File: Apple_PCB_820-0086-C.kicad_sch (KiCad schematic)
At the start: 0 parts

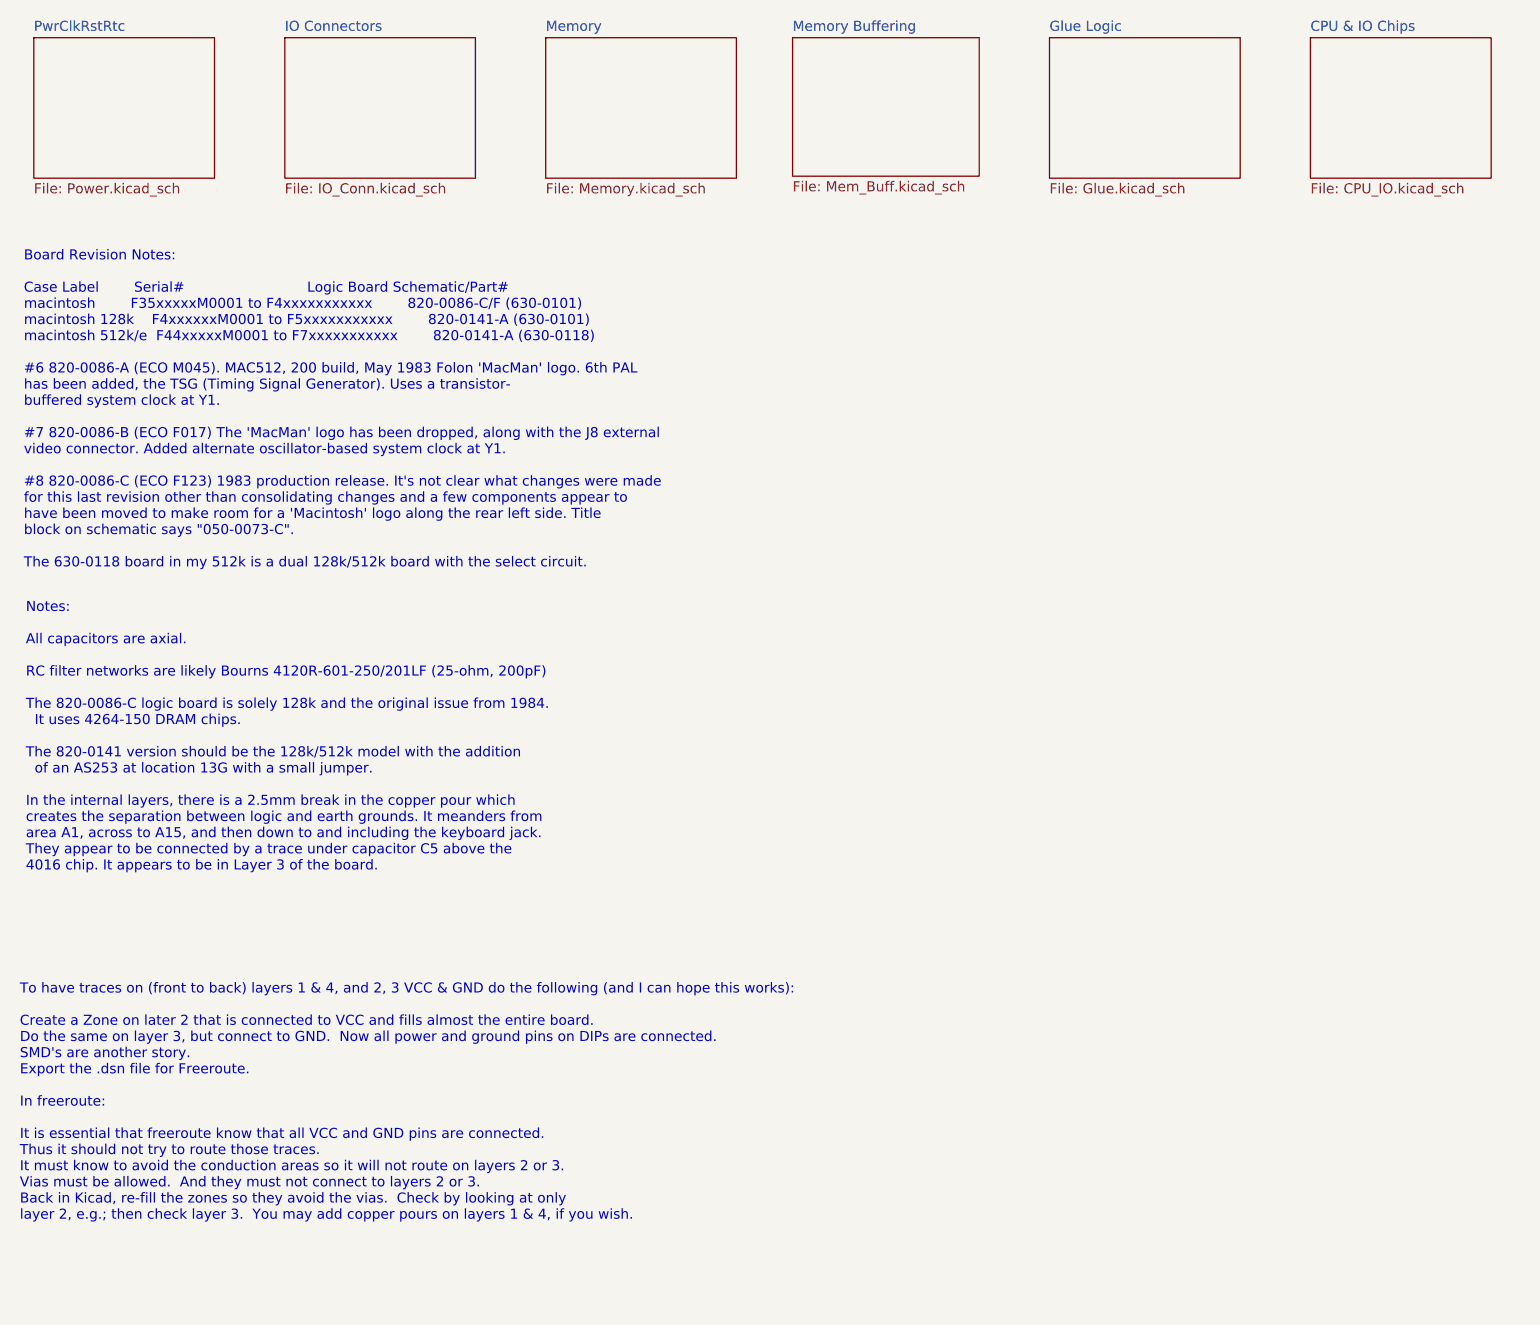
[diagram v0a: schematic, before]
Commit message: Add files via upload
After obtaining actual  128k board, certain component placement tweaks were made. Board was re-routed based on those changes.
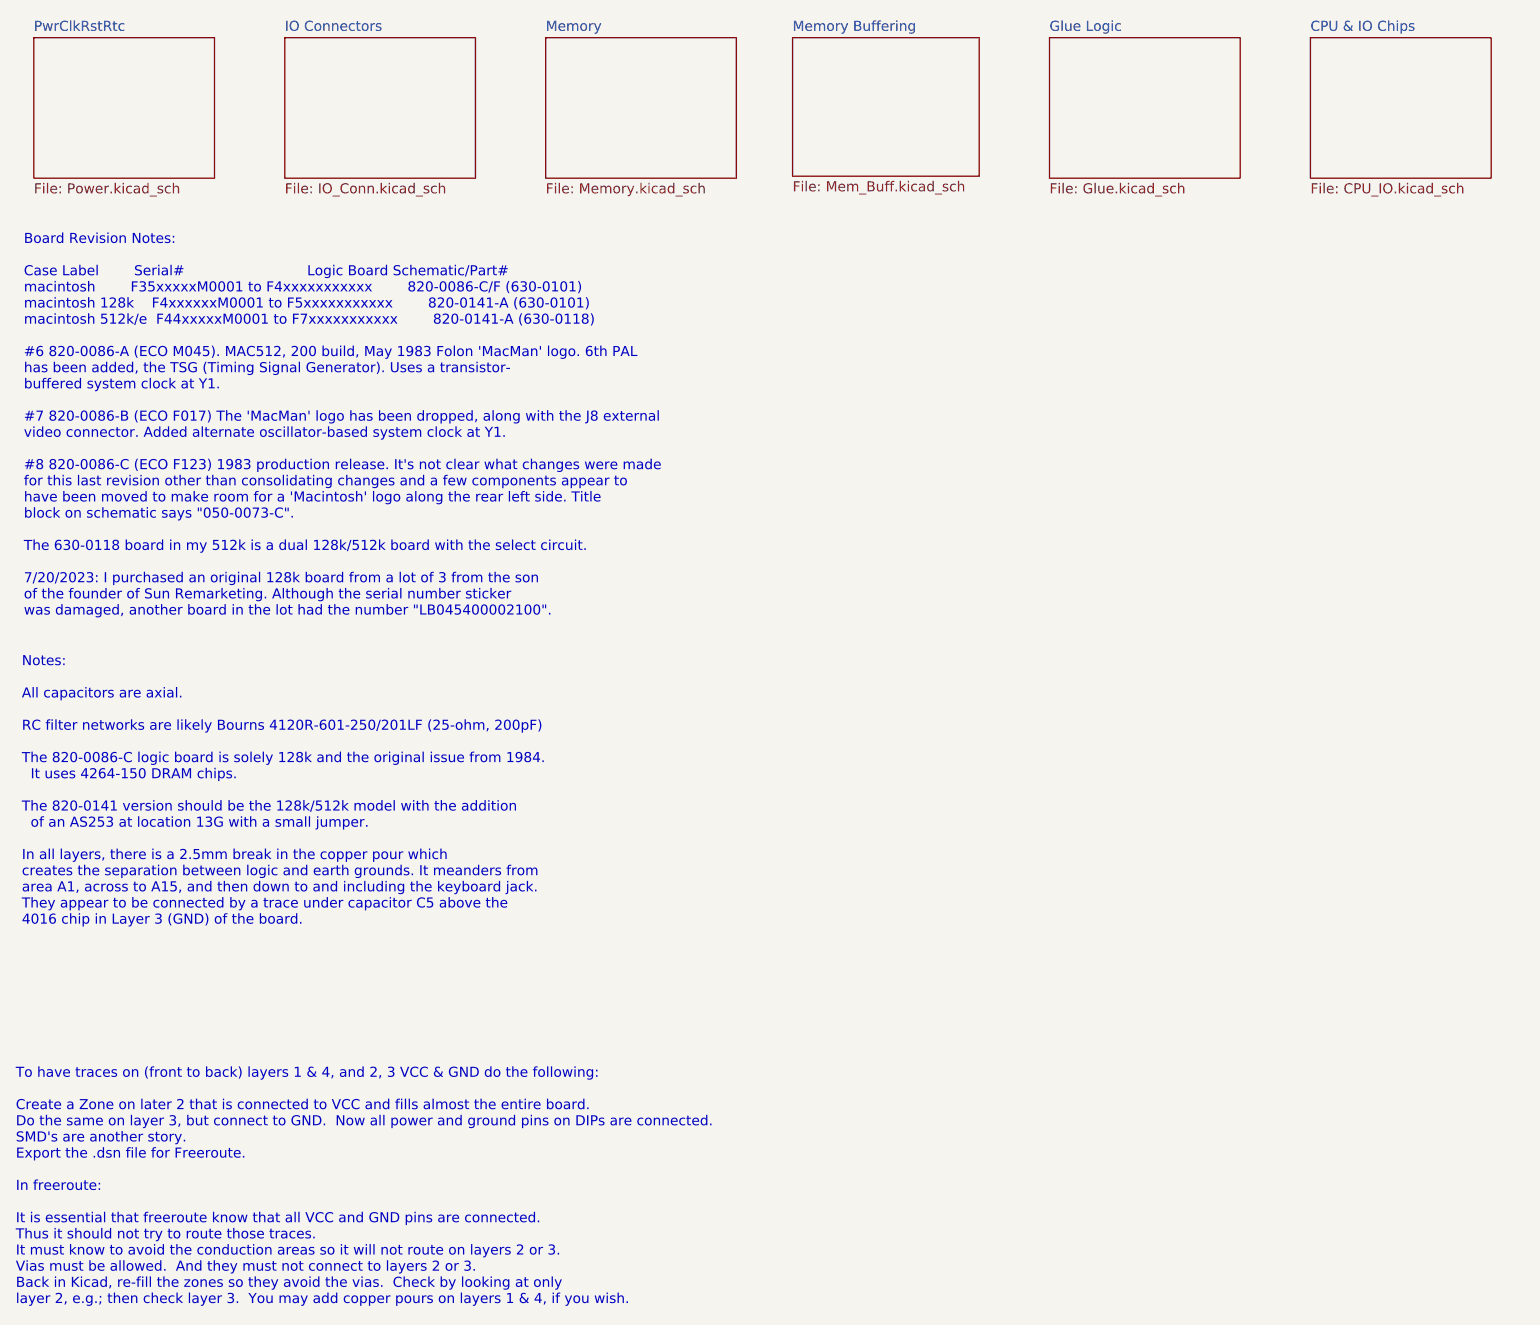
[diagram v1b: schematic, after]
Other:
- note added: "Notes: All capacitors are axial. RC filter networks are likely Bourns 4120R-601-250/201LF (25-ohm, 200pF) The 820-0086-C logic board is solely 128k and the original issue from 1984. It uses 4264-150 DRAM chips. The 820-0141 version should be the 128k/512k model with the addition of an AS253 at location 13G with a small jumper. In all layers, there is a 2.5mm break in the copper pour which creates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"
- note added: "To have traces on (front to back) layers 1 & 4, and 2, 3 VCC & GND do the following: Create a Zone on later 2 that is connected to VCC and fills almost the entire board. Do the same on layer 3, but connect to GND. Now all power and ground pins on DIPs are connected. SMD's are another story. Export the .dsn file for Freeroute. In freeroute: It is essential that freeroute know that all VCC and GND 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"
- note removed: "Notes: All capacitors are axial. RC filter networks are likely Bourns 4120R-601-250/201LF (25-ohm, 200pF) The 820-0086-C logic board is solely 128k and the original issue from 1984. It uses 4264-150 DRAM chips. The 820-0141 version should be the 128k/512k model with the addition of an AS253 at location 13G with a small jumper. In the internal layers, there is a 2.5mm break in the copper pour whic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"
- note removed: "To have traces on (front to back) layers 1 & 4, and 2, 3 VCC & GND do the following (and I can hope this works): Create a Zone on later 2 that is connected to VCC and fills almost the entire board. Do the same on layer 3, but connect to GND. Now all power and ground pins on DIPs are connected. SMD's are another story. Export the .dsn file for Freeroute. In freeroute: It is essential that freerout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"
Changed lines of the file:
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@@
     (comment 2 "Release")
   )
-  (text "Board Revision Notes:\n\nCase Label		Serial#							Logic Board Schematic/Part#\nmacintosh		F35xxxxxM0001 to F4xxxxxxxxxxx        820-0086-C/F (630-0101)\nmacintosh 128k	F4xxxxxxM0001 to F5xxxxxxxxxxx        820-0141-A (630-0101)\nmacintosh 512k/e  F44xxxxxM0001 to F7xxxxxxxxxxx        820-0141-A (630-0118)\n\n#6 820-0086-A (ECO M045). MAC512, 200 build, May 1983 Folon 'MacMan' logo. 6th PAL\nhas been added, the TSG (Timing Signal Generator). Uses a transistor-\nbuffered system clock at Y1.\n\n#7 820-0086-B (ECO F017) The 'MacMan' logo has been dropped, along with the J8 external\nvideo connector. Added alternate oscillator-based system clock at Y1.\n\n#8 820-0086-C (ECO F123) 1983 production release. It's not clear what changes were made\nfor this last revision other than consolidating changes and a few components appear to \nhave been moved to make room for a 'Macintosh' logo along the rear left side. Title\nblock on schematic says \"050-0073-C\".\n\nThe 630-0118 board in my 512k is a dual 128k/512k board with the select circuit."
-    (at 19.05 88.9 0)
+  (text "Board Revision Notes:\n\nCase Label		Serial#							Logic Board Schematic/Part#\nmacintosh		F35xxxxxM0001 to F4xxxxxxxxxxx        820-0086-C/F (630-0101)\nmacintosh 128k	F4xxxxxxM0001 to F5xxxxxxxxxxx        820-0141-A (630-0101)\nmacintosh 512k/e  F44xxxxxM0001 to F7xxxxxxxxxxx        820-0141-A (630-0118)\n\n#6 820-0086-A (ECO M045). MAC512, 200 build, May 1983 Folon 'MacMan' logo. 6th PAL\nhas been added, the TSG (Timing Signal Generator). Uses a transistor-\nbuffered system clock at Y1.\n\n#7 820-0086-B (ECO F017) The 'MacMan' logo has been dropped, along with the J8 external\nvideo connector. Added alternate oscillator-based system clock at Y1.\n\n#8 820-0086-C (ECO F123) 1983 production release. It's not clear what changes were made\nfor this last revision other than consolidating changes and a few components appear to \nhave been moved to make room for a 'Macintosh' logo along the rear left side. Title\nblock on schematic says \"050-0073-C\".\n\nThe 630-0118 board in my 512k is a dual 128k/512k board with the select circuit.\n\n7/20/2023: I purchased an original 128k board from a lot of 3 from the son\nof the founder of Sun Remarketing. Although the serial number sticker\nwas damaged, another board in the lot had the number \"LB045400002100\".\n"
+    (at 19.05 94.996 0)
     (effects (font (size 1.27 1.27)) (justify left bottom))
   )
-  (text "To have traces on (front to back) layers 1 & 4, and 2, 3 VCC & GND do the following (and I can hope this works):\n\nCreate a Zone on later 2 that is connected to VCC and fills almost the entire board.\nDo the same on layer 3, but connect to GND.  Now all power and ground pins on DIPs are connected.  \nSMD's are another story.\nExport the .dsn file for Freeroute.\n\nIn freeroute:\n\nIt is essential that freeroute know that all VCC and GND pins are connected.  \nThus it should not try to route those traces.\nIt must know to avoid the conduction areas so it will not route on layers 2 or 3.\nVias must be allowed.  And they must not connect to layers 2 or 3.\nBack in Kicad, re-fill the zones so they avoid the vias.  Check by looking at only \nlayer 2, e.g.; then check layer 3.  You may add copper pours on layers 1 & 4, if you wish."
-    (at 18.542 171.45 0)
+  (text "To have traces on (front to back) layers 1 & 4, and 2, 3 VCC & GND do the following:\n\nCreate a Zone on later 2 that is connected to VCC and fills almost the entire board.\nDo the same on layer 3, but connect to GND.  Now all power and ground pins on DIPs are connected.  \nSMD's are another story.\nExport the .dsn file for Freeroute.\n\nIn freeroute:\n\nIt is essential that freeroute know that all VCC and GND pins are connected.  \nThus it should not try to route those traces.\nIt must know to avoid the conduction areas so it will not route on layers 2 or 3.\nVias must be allowed.  And they must not connect to layers 2 or 3.\nBack in Kicad, re-fill the zones so they avoid the vias.  Check by looking at only \nlayer 2, e.g.; then check layer 3.  You may add copper pours on layers 1 & 4, if you wish."
+    (at 18.034 182.118 0)
     (effects (font (size 1.27 1.27)) (justify left bottom))
   )
-  (text "Notes:\n\nAll capacitors are axial.\n\nRC filter networks are likely Bourns 4120R-601-250/201LF (25-ohm, 200pF)\n\nThe 820-0086-C logic board is solely 128k and the original issue from 1984.\n  It uses 4264-150 DRAM chips. \n\nThe 820-0141 version should be the 128k/512k model with the addition\n  of an AS253 at location 13G with a small jumper.\n\nIn the internal layers, there is a 2.5mm break in the copper pour which\ncreates the separation between logic and earth grounds. It meanders from\narea A1, across to A15, and then down to and including the keyboard jack.\nThey appear to be connected by a trace under capacitor C5 above the\n4016 chip. It appears to be in Layer 3 of the board."
-    (at 19.304 127.254 0)
+  (text "Notes:\n\nAll capacitors are axial.\n\nRC filter networks are likely Bourns 4120R-601-250/201LF (25-ohm, 200pF)\n\nThe 820-0086-C logic board is solely 128k and the original issue from 1984.\n  It uses 4264-150 DRAM chips. \n\nThe 820-0141 version should be the 128k/512k model with the addition\n  of an AS253 at location 13G with a small jumper.\n\nIn all layers, there is a 2.5mm break in the copper pour which\ncreates the separation between logic and earth grounds. It meanders from\narea A1, across to A15, and then down to and including the keyboard jack.\nThey appear to be connected by a trace under capacitor C5 above the\n4016 chip in Layer 3 (GND) of the board."
+    (at 18.796 134.112 0)
     (effects (font (size 1.27 1.27)) (justify left bottom))
   )
@@
     )
     (path "/ae841087-0a6c-4684-b14f-9b2edf1c52e9/e6323431-a393-47df-be2c-6954907dd23a"
-      (reference "C5") (unit 1) (value "33uF") (footprint "Capacitor_THT:CP_Axial_L11.0mm_D6.0mm_P18.00mm_Horizontal")
+      (reference "C5") (unit 1) (value "33uF") (footprint "Capacitor_THT:CP_Axial_L11.0mm_D5.0mm_P18.00mm_Horizontal")
     )
     (path "/de4fdae0-41e4-4194-88b4-8ae352cf053f/d5e23db5-a9fe-4a11-aaea-2f60503c0d9d"
@@
     )
     (path "/ae841087-0a6c-4684-b14f-9b2edf1c52e9/d56790fc-0ad5-4165-a5f1-08a0a267882a"
-      (reference "C20") (unit 1) (value "33uF") (footprint "Capacitor_THT:CP_Axial_L11.0mm_D6.0mm_P18.00mm_Horizontal")
+      (reference "C20") (unit 1) (value "33uF") (footprint "Capacitor_THT:CP_Axial_L11.0mm_D5.0mm_P18.00mm_Horizontal")
     )
     (path "/ae841087-0a6c-4684-b14f-9b2edf1c52e9/cbfceff7-3385-443e-95ee-7d2fccfdfbc4"
-      (reference "C21") (unit 1) (value ".1uF") (footprint "Capacitor_THT:C_Axial_L5.1mm_D3.1mm_P10.00mm_Horizontal")
+      (reference "C21") (unit 1) (value ".1uF") (footprint "Capacitor_THT:C_Axial_L3.8mm_D2.6mm_P7.50mm_Horizontal")
     )
     (path "/ae841087-0a6c-4684-b14f-9b2edf1c52e9/181ddae1-ce75-4ebc-8c68-18283bfc60f8"
@@
     )
     (path "/ae841087-0a6c-4684-b14f-9b2edf1c52e9/5b707f0b-8f0d-46d2-8528-392da835298c"
-      (reference "H201") (unit 1) (value "MountingHole_Pad") (footprint "MountingHole:MountingHole_2.7mm_M2.5_Pad")
+      (reference "H201") (unit 1) (value "MountingHole_Pad") (footprint "TestPoint:TestPoint_Plated_Hole_D2.0mm")
     )
     (path "/ae841087-0a6c-4684-b14f-9b2edf1c52e9/c10dfd53-18da-45d9-b7ef-9b98035f26b7"
-      (reference "H202") (unit 1) (value "MountingHole_Pad") (footprint "MountingHole:MountingHole_2.7mm_M2.5_Pad")
+      (reference "H202") (unit 1) (value "MountingHole_Pad") (footprint "TestPoint:TestPoint_Plated_Hole_D2.0mm")
     )
     (path "/ae841087-0a6c-4684-b14f-9b2edf1c52e9/ce27f151-3327-4c42-816b-e93a8e2afe9f"
-      (reference "H203") (unit 1) (value "MountingHole_Pad") (footprint "MountingHole:MountingHole_2.7mm_M2.5_Pad")
+      (reference "H203") (unit 1) (value "MountingHole_Pad") (footprint "TestPoint:TestPoint_Plated_Hole_D2.0mm")
     )
     (path "/ae841087-0a6c-4684-b14f-9b2edf1c52e9/17ce8d76-a104-427d-a056-2425c14fb057"
-      (reference "H204") (unit 1) (value "MountingHole_Pad") (footprint "MountingHole:MountingHole_2.7mm_M2.5_Pad")
+      (reference "H204") (unit 1) (value "MountingHole_Pad") (footprint "TestPoint:TestPoint_Plated_Hole_D2.0mm")
     )
     (path "/ae841087-0a6c-4684-b14f-9b2edf1c52e9/c74d1f55-f041-4574-b904-8bfd712e8128"
-      (reference "H205") (unit 1) (value "MountingHole_Pad") (footprint "MountingHole:MountingHole_2.7mm_M2.5_Pad")
+      (reference "H205") (unit 1) (value "MountingHole_Pad") (footprint "TestPoint:TestPoint_Plated_Hole_D2.0mm")
     )
     (path "/ae841087-0a6c-4684-b14f-9b2edf1c52e9/81974273-6ec9-4e36-b7a5-6da69181751d"
-      (reference "H206") (unit 1) (value "MountingHole_Pad") (footprint "MountingHole:MountingHole_2.7mm_M2.5_Pad")
+      (reference "H206") (unit 1) (value "MountingHole_Pad") (footprint "TestPoint:TestPoint_Plated_Hole_D2.0mm")
     )
     (path "/ae841087-0a6c-4684-b14f-9b2edf1c52e9/87280b50-0c3c-41fe-add1-ac0e0db65994"
-      (reference "H207") (unit 1) (value "MountingHole_Pad") (footprint "MountingHole:MountingHole_2.7mm_M2.5_Pad")
+      (reference "H207") (unit 1) (value "MountingHole_Pad") (footprint "TestPoint:TestPoint_Plated_Hole_D2.0mm")
     )
     (path "/ae841087-0a6c-4684-b14f-9b2edf1c52e9/07966900-9ab2-411a-8b53-5c234d0787c8"
-      (reference "H208") (unit 1) (value "MountingHole_Pad") (footprint "MountingHole:MountingHole_2.7mm_M2.5_Pad")
+      (reference "H208") (unit 1) (value "MountingHole_Pad") (footprint "TestPoint:TestPoint_Plated_Hole_D2.0mm")
     )
     (path "/ae841087-0a6c-4684-b14f-9b2edf1c52e9/3236da5b-1a8c-474d-a999-c9d6840b1109"
